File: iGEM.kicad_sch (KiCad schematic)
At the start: 49 parts, among them IC1 TMCS1107A1BQDRQ1, IC2 MCP4561-502E_MS, IC3 SN74LVC2G08IDCTRQ1, J1 COIL1, J2 Conn_01x03, J3 Conn_01x02, J4 Conn_01x03, J5 Conn_01x03, J6 Conn_02x03_Odd_Even, M1 Fan, Q1 TIP122, Q2 IPD042P03L3GATMA1, Q3 IPD042P03L3GATMA1, Q4 D44VH, Q5 IPD042P03L3GATMA1, Q6 IPD042P03L3GATMA1, U1 ADC101C021CIMK, U2 ATtiny412-SS, U3 SN74LVC1G04DBVR, U4 MD1211, U5 MD1211

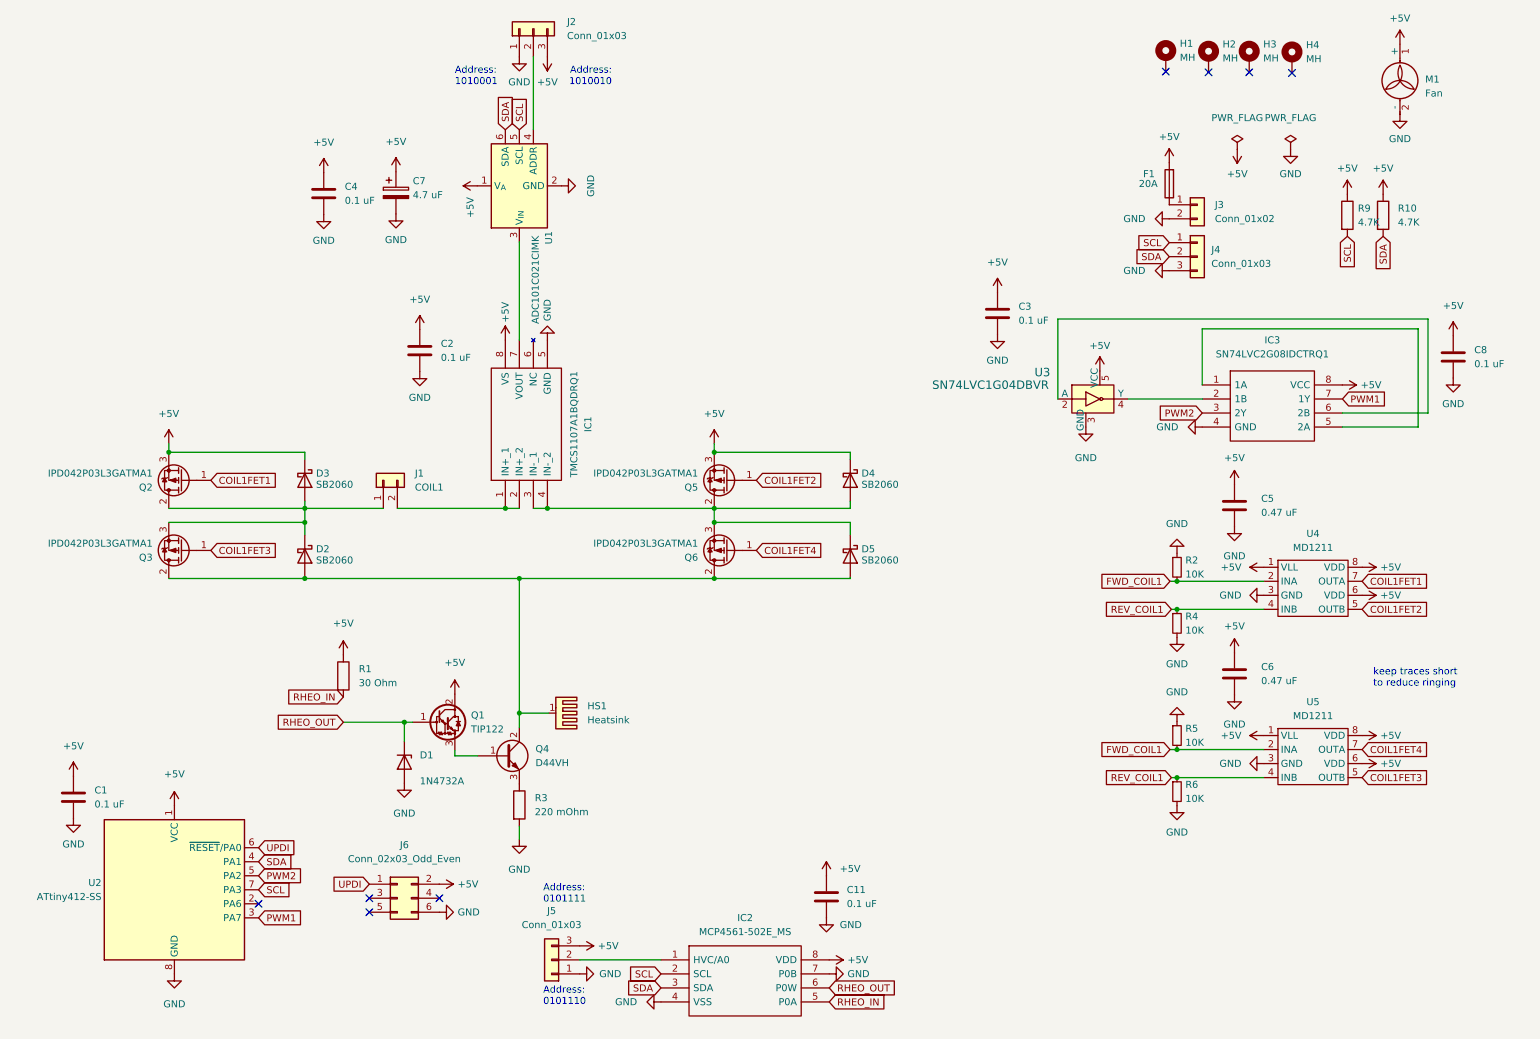
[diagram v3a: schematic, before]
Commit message: Added indicator LED and updated resistor value
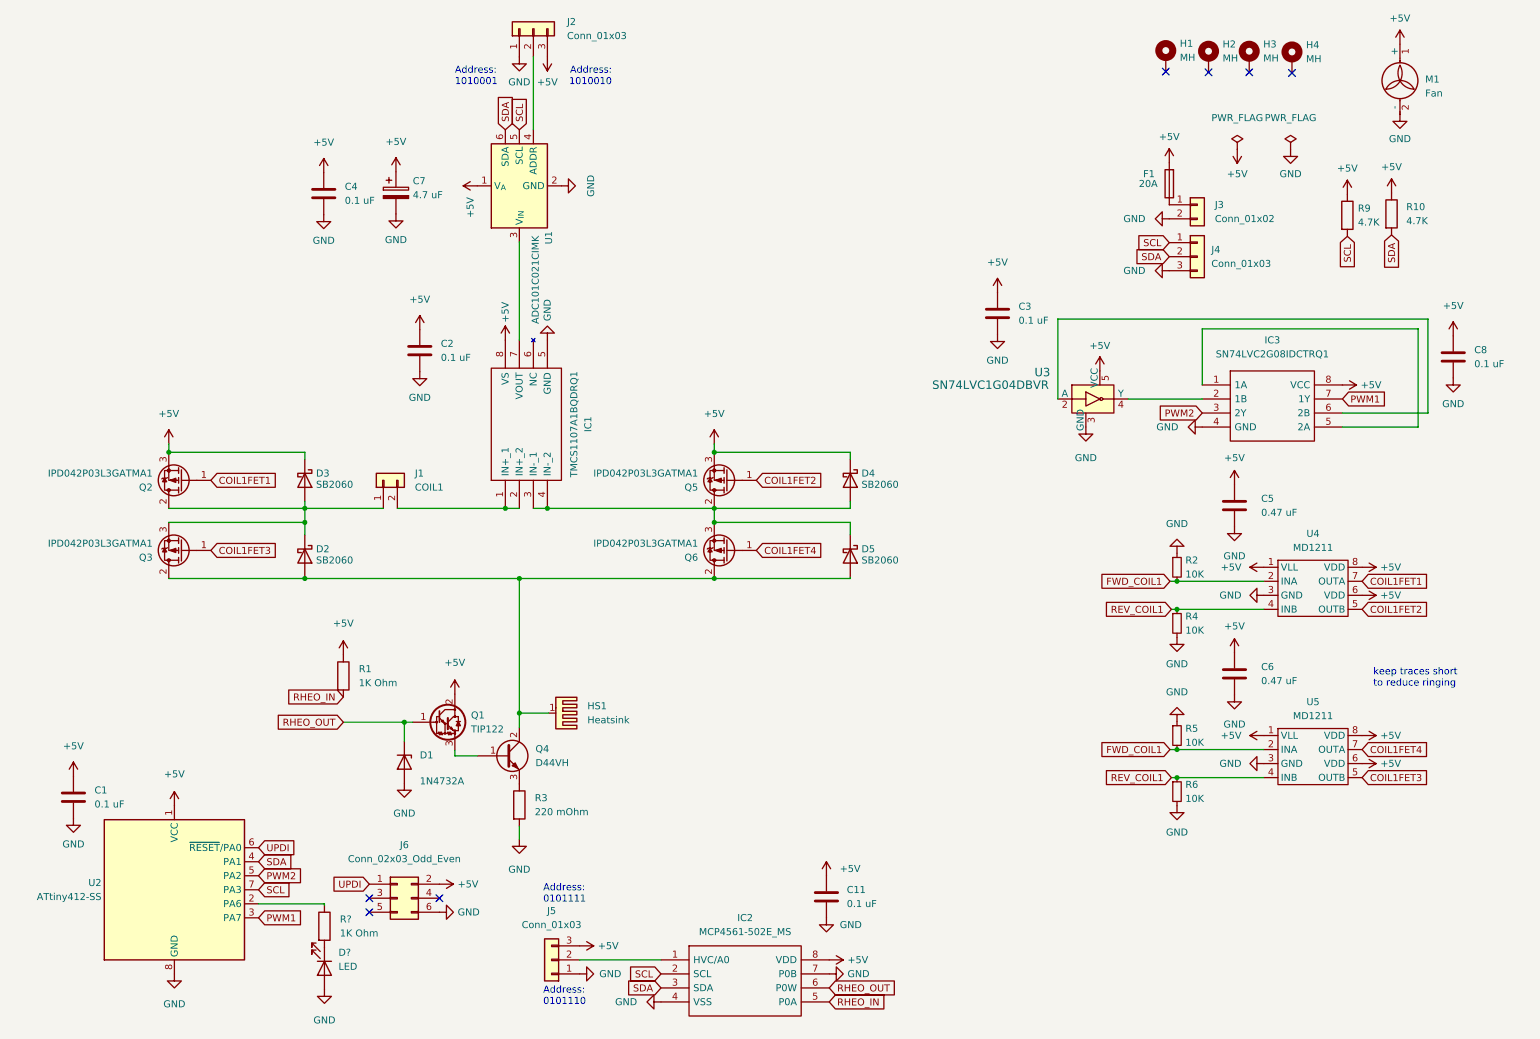
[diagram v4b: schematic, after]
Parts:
- added D?: LED, LED_SMD:LED_0805_2012Metric_Pad1.15x1.40mm_HandSolder, symbol Device:LED
- added R?: 1K Ohm, Resistor_SMD:R_0805_2012Metric_Pad1.20x1.40mm_HandSolder, symbol Device:R
- R1: value 30 Ohm -> 1K Ohm; footprint Capacitor_SMD:C_0805_2012Metric_Pad1.18x1.45mm_HandSolder -> Resistor_SMD:R_0805_2012Metric_Pad1.20x1.40mm_HandSolder; DigiKey RMCF0805FT30R0CT-ND -> CHP0805-FX-1001ELFCT-ND
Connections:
- net GND: now also D?.2 (A)
- net at U2.2 (PA6): now also R?.1
- new net: D?.1 (K), R?.2
- no-connect marks 8 -> 7
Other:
- moved on the sheet: R10
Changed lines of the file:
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@@
   (no_connect (at 236.093 24.638))
   (no_connect (at 243.84 24.765))
-  (no_connect (at 56.642 175.26))
   (wire (pts (xy 114.808 185.42) (xy 129.54 185.42))
     (stroke (width 0) (type default) (color 0 0 0 0))
@@
     (stroke (width 0) (type default) (color 0 0 0 0))
   )
+  (wire (pts (xy 68.58 175.26) (xy 68.58 175.514))
+    (stroke (width 0) (type default) (color 0 0 0 0))
+  )
   (wire (pts (xy 65.024 103.632) (xy 65.024 106.172))
     (stroke (width 0) (type default) (color 0 0 0 0))
@@
   )
   (wire (pts (xy 221.996 121.92) (xy 223.012 121.92))
+    (stroke (width 0) (type default) (color 0 0 0 0))
+  )
+  (wire (pts (xy 56.642 175.26) (xy 68.58 175.26))
     (stroke (width 0) (type default) (color 0 0 0 0))
   )
@@
     )
   )
-  (global_label "SDA" (shape input) (at 260.35 54.356 270) (fields_autoplaced)
+  (global_label "SDA" (shape input) (at 261.874 54.102 270) (fields_autoplaced)
     (effects (font (size 1.27 1.27)) (justify right))
-    (property "Intersheet References" "${INTERSHEET_REFS}" (id 0) (at 260.2706 60.3372 90)
+    (property "Intersheet References" "${INTERSHEET_REFS}" (id 0) (at 261.7946 60.0832 90)
       (effects (font (size 1.27 1.27)) (justify right) hide)
     )
@@
     (pin "3")
   )
-  (symbol (lib_id "Device:R") (at 260.35 50.546 0) (unit 1)
-    (in_bom yes) (on_board yes) (fields_autoplaced)
-    (property "Reference" "R10" (id 0) (at 263.017 49.2759 0)
-      (effects (font (size 1.27 1.27)) (justify left))
-    )
-    (property "Value" "4.7K" (id 1) (at 263.017 51.8159 0)
-      (effects (font (size 1.27 1.27)) (justify left))
-    )
-    (property "Footprint" "Resistor_SMD:R_0805_2012Metric_Pad1.20x1.40mm_HandSolder" (id 2) (at 258.572 50.546 90)
-      (effects (font (size 1.27 1.27)) hide)
-    )
-    (property "Datasheet" "~" (id 3) (at 260.35 50.546 0)
-      (effects (font (size 1.27 1.27)) hide)
-    )
-    (property "DigiKey" "RMCF0805FT4K70CT-ND" (id 4) (at 260.35 50.546 0)
+  (symbol (lib_id "Device:R") (at 261.874 50.292 0) (unit 1)
+    (in_bom yes) (on_board yes) (fields_autoplaced)
+    (property "Reference" "R10" (id 0) (at 264.541 49.0219 0)
+      (effects (font (size 1.27 1.27)) (justify left))
+    )
+    (property "Value" "4.7K" (id 1) (at 264.541 51.5619 0)
+      (effects (font (size 1.27 1.27)) (justify left))
+    )
+    (property "Footprint" "Resistor_SMD:R_0805_2012Metric_Pad1.20x1.40mm_HandSolder" (id 2) (at 260.096 50.292 90)
+      (effects (font (size 1.27 1.27)) hide)
+    )
+    (property "Datasheet" "~" (id 3) (at 261.874 50.292 0)
+      (effects (font (size 1.27 1.27)) hide)
+    )
+    (property "DigiKey" "RMCF0805FT4K70CT-ND" (id 4) (at 261.874 50.292 0)
       (effects (font (size 1.27 1.27)) hide)
     )
@@
     )
     (pin "1")
+  )
+  (symbol (lib_id "Device:LED") (at 68.58 186.944 270) (unit 1)
+    (in_bom yes) (on_board yes) (fields_autoplaced)
+    (property "Reference" "D?" (id 0) (at 71.12 184.0864 90)
+      (effects (font (size 1.27 1.27)) (justify left))
+    )
+    (property "Value" "LED" (id 1) (at 71.12 186.6264 90)
+      (effects (font (size 1.27 1.27)) (justify left))
+    )
+    (property "Footprint" "LED_SMD:LED_0805_2012Metric_Pad1.15x1.40mm_HandSolder" (id 2) (at 68.58 186.944 0)
+      (effects (font (size 1.27 1.27)) hide)
+    )
+    (property "Datasheet" "~" (id 3) (at 68.58 186.944 0)
+      (effects (font (size 1.27 1.27)) hide)
+    )
+    (property "DigiKey" "475-1410-1-ND" (id 4) (at 68.58 186.944 90)
+      (effects (font (size 1.27 1.27)) hide)
+    )
+    (pin "1")
+    (pin "2")
   )
   (symbol (lib_name "MD1211_1") (lib_id "MD1211:MD1211") (at 247.65 118.11 0) (unit 1)
@@
     (pin "2")
   )
-  (symbol (lib_id "power:+5V") (at 260.35 46.736 0) (unit 1)
+  (symbol (lib_id "power:+5V") (at 261.874 46.482 0) (unit 1)
     (in_bom yes) (on_board yes)
-    (property "Reference" "#PWR0119" (id 0) (at 260.35 50.546 0)
-      (effects (font (size 1.27 1.27)) hide)
-    )
-    (property "Value" "+5V" (id 1) (at 260.35 42.037 0))
-    (property "Footprint" "" (id 2) (at 260.35 46.736 0)
-      (effects (font (size 1.27 1.27)) hide)
-    )
-    (property "Datasheet" "" (id 3) (at 260.35 46.736 0)
+    (property "Reference" "#PWR0119" (id 0) (at 261.874 50.292 0)
+      (effects (font (size 1.27 1.27)) hide)
+    )
+    (property "Value" "+5V" (id 1) (at 261.874 41.783 0))
+    (property "Footprint" "" (id 2) (at 261.874 46.482 0)
+      (effects (font (size 1.27 1.27)) hide)
+    )
+    (property "Datasheet" "" (id 3) (at 261.874 46.482 0)
       (effects (font (size 1.27 1.27)) hide)
     )
@@
       (effects (font (size 1.27 1.27)) (justify left))
     )
-    (property "Value" "30 Ohm" (id 1) (at 74.803 135.2549 0)
-      (effects (font (size 1.27 1.27)) (justify left))
-    )
-    (property "Footprint" "Capacitor_SMD:C_0805_2012Metric_Pad1.18x1.45mm_HandSolder" (id 2) (at 70.231 133.985 90)
+    (property "Value" "1K Ohm" (id 1) (at 74.803 135.2549 0)
+      (effects (font (size 1.27 1.27)) (justify left))
+    )
+    (property "Footprint" "Resistor_SMD:R_0805_2012Metric_Pad1.20x1.40mm_HandSolder" (id 2) (at 70.231 133.985 90)
       (effects (font (size 1.27 1.27)) hide)
     )
@@
       (effects (font (size 1.27 1.27)) hide)
     )
-    (property "DigiKey" "RMCF0805FT30R0CT-ND" (id 4) (at 72.009 133.985 0)
+    (property "DigiKey" "CHP0805-FX-1001ELFCT-ND" (id 4) (at 72.009 133.985 0)
       (effects (font (size 1.27 1.27)) hide)
     )
@@
     (pin "1")
   )
+  (symbol (lib_id "power:GND") (at 68.58 190.754 0) (unit 1)
+    (in_bom yes) (on_board yes) (fields_autoplaced)
+    (property "Reference" "#PWR?" (id 0) (at 68.58 197.104 0)
+      (effects (font (size 1.27 1.27)) hide)
+    )
+    (property "Value" "GND" (id 1) (at 68.58 196.342 0))
+    (property "Footprint" "" (id 2) (at 68.58 190.754 0)
+      (effects (font (size 1.27 1.27)) hide)
+    )
+    (property "Datasheet" "" (id 3) (at 68.58 190.754 0)
+      (effects (font (size 1.27 1.27)) hide)
+    )
+    (pin "1")
+  )
   (symbol (lib_id "power:+5V") (at 256.54 119.38 270) (unit 1)
     (in_bom yes) (on_board yes) (fields_autoplaced)
@@
     (pin "1")
   )
+  (symbol (lib_id "Device:R") (at 68.58 179.324 0) (unit 1)
+    (in_bom yes) (on_board yes) (fields_autoplaced)
+    (property "Reference" "R?" (id 0) (at 71.374 178.0539 0)
+      (effects (font (size 1.27 1.27)) (justify left))
+    )
+    (property "Value" "1K Ohm" (id 1) (at 71.374 180.5939 0)
+      (effects (font (size 1.27 1.27)) (justify left))
+    )
+    (property "Footprint" "Resistor_SMD:R_0805_2012Metric_Pad1.20x1.40mm_HandSolder" (id 2) (at 66.802 179.324 90)
+      (effects (font (size 1.27 1.27)) hide)
+    )
+    (property "Datasheet" "~" (id 3) (at 68.58 179.324 0)
+      (effects (font (size 1.27 1.27)) hide)
+    )
+    (property "DigiKey" "CHP0805-FX-1001ELFCT-ND" (id 4) (at 68.58 179.324 0)
+      (effects (font (size 1.27 1.27)) hide)
+    )
+    (pin "1")
+    (pin "2")
+  )
   (symbol (lib_id "power:GND") (at 89.408 176.784 90) (unit 1)
     (in_bom yes) (on_board yes) (fields_autoplaced)
@@
       (reference "#PWR0131") (unit 1) (value "GND") (footprint "")
     )
+    (path "/c7e90eee-2fb5-4f34-8810-8edfe8f37c3a"
+      (reference "#PWR?") (unit 1) (value "GND") (footprint "")
+    )
     (path "/0fbdd8b7-d3db-4cb1-9102-673f223a760c"
       (reference "C1") (unit 1) (value "0.1 uF") (footprint "Capacitor_SMD:C_0805_2012Metric_Pad1.18x1.45mm_HandSolder")
@@
       (reference "D5") (unit 1) (value "SB2060") (footprint "Diode_THT:D_DO-201AD_P12.70mm_Horizontal")
     )
+    (path "/5327e8bf-ae82-4039-9cd4-8576c3288851"
+      (reference "D?") (unit 1) (value "LED") (footprint "LED_SMD:LED_0805_2012Metric_Pad1.15x1.40mm_HandSolder")
+    )
     (path "/eadcb800-30ab-4a2d-bc96-28b421a136a3"
       (reference "F1") (unit 1) (value "20A") (footprint "Fuse:Fuseholder_Blade_Mini_Keystone_3568")
@@
     )
     (path "/9dbd19f4-6a66-4910-871d-92295a4321e7"
-      (reference "R1") (unit 1) (value "30 Ohm") (footprint "Capacitor_SMD:C_0805_2012Metric_Pad1.18x1.45mm_HandSolder")
+      (reference "R1") (unit 1) (value "1K Ohm") (footprint "Resistor_SMD:R_0805_2012Metric_Pad1.20x1.40mm_HandSolder")
     )
     (path "/82e4ca13-c8a3-4875-a498-8c74cd9a9fd2"
@@
       (reference "R10") (unit 1) (value "4.7K") (footprint "Resistor_SMD:R_0805_2012Metric_Pad1.20x1.40mm_HandSolder")
     )
+    (path "/e621144d-f4f0-4ed0-afcb-e43069706fe3"
+      (reference "R?") (unit 1) (value "1K Ohm") (footprint "Resistor_SMD:R_0805_2012Metric_Pad1.20x1.40mm_HandSolder")
+    )
     (path "/69a61c1d-1543-4184-a789-f583b0735f7e"

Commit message: added bulk capacitance and bug fixes
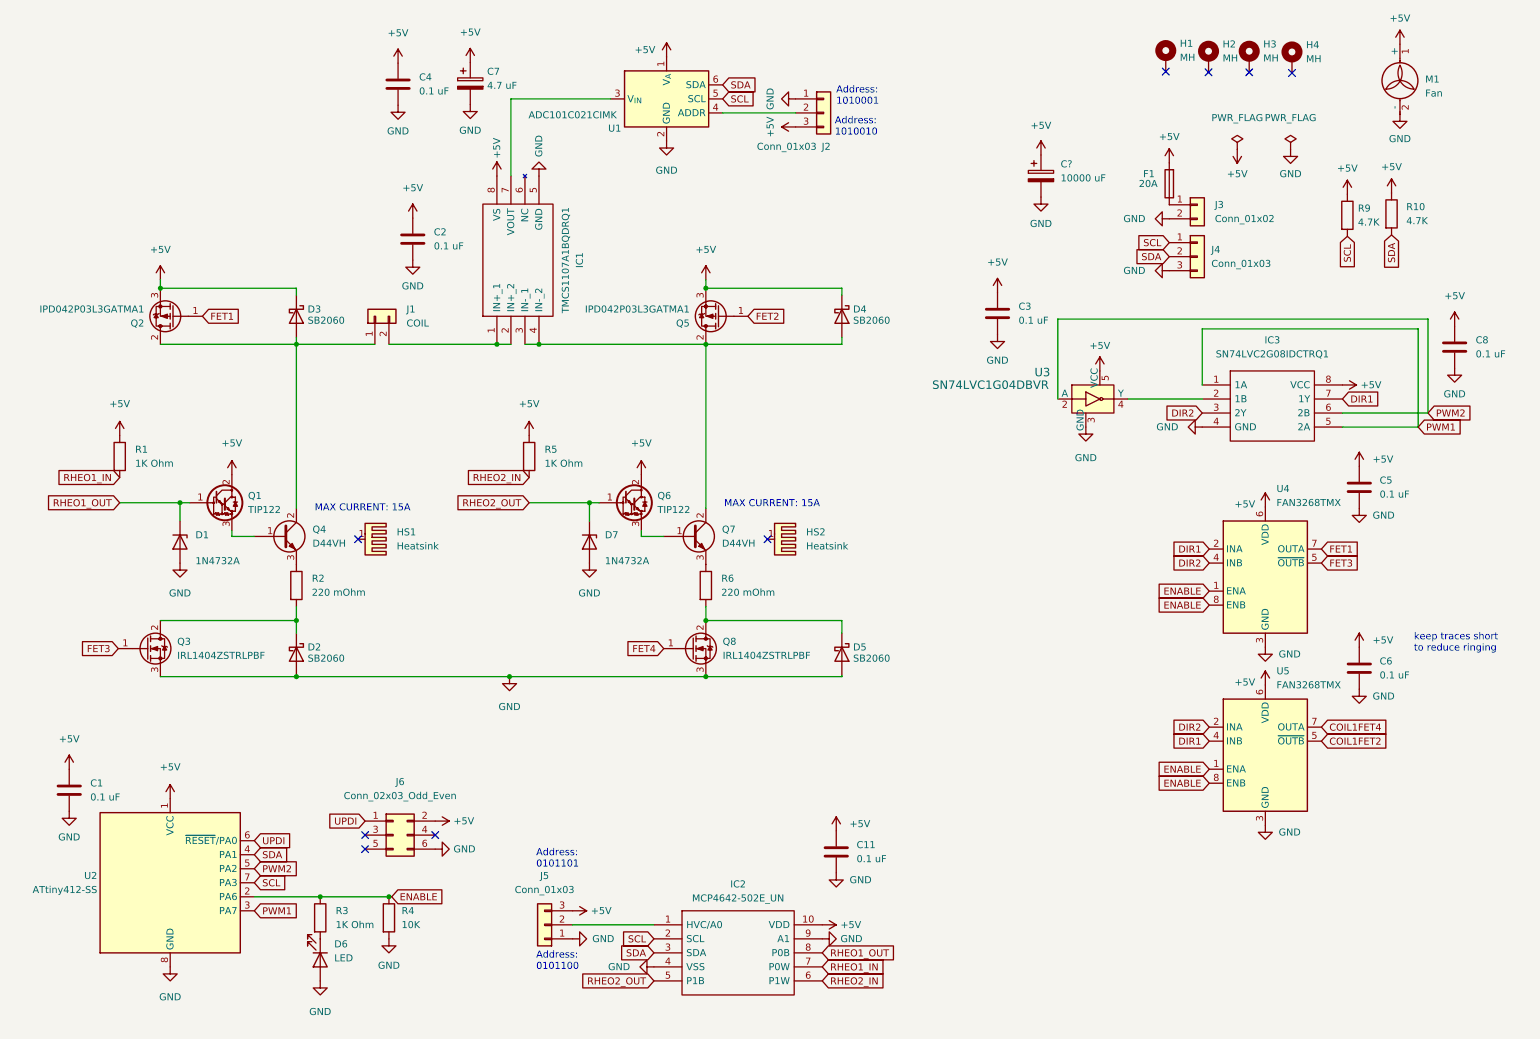
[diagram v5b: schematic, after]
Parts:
- removed IC2: MCP4561-502E_MS, Package_SO:MSOP-8_3x3mm_P0.65mm, symbol MCP4561-502E_MS:MCP4561-502E_MS
- removed Q3, Q6: IPD042P03L3GATMA1, Package_TO_SOT_SMD:TO-252-2, symbol Device:Q_PMOS_GDS
- removed R2, R4, R5, R6: 10K, Capacitor_SMD:C_0805_2012Metric_Pad1.18x1.45mm_HandSolder, symbol Device:R_Small
- removed R3: 220 mOhm, TerminalBlock:TerminalBlock_bornier-2_P5.08mm, symbol Device:R
- removed U4, U5: MD1211, Package_SO:SOIC-8_3.9x4.9mm_P1.27mm, symbol MD1211:MD1211
- added C?: 10000 uF, Capacitor_THT:CP_Radial_D22.0mm_P10.00mm_SnapIn, symbol Device:C_Polarized
- added D7: 1N4732A, Diode_THT:D_DO-41_SOD81_P10.16mm_Horizontal, symbol Diode:1N47xxA
- added HS2: Heatsink, Heatsink:Heatsink_AAVID_576802B03900G, symbol Mechanical:Heatsink_Pad
- added IC2: MCP4642-502E_UN, SOP50P490X110-10N, symbol MCP4642-502E_UN:MCP4642-502E_UN
- added Q3, Q8: IRL1404ZSTRLPBF, Package_TO_SOT_SMD:TO-263-2, symbol Device:Q_NMOS_GDS
- added Q6: TIP122, Package_TO_SOT_THT:TO-220-3_Vertical, symbol Transistor_BJT:TIP122
- added Q7: D44VH, Package_TO_SOT_THT:TO-220-3_Vertical, symbol Device:Q_NPN_BCE
- added R2, R6: 220 mOhm, TerminalBlock:TerminalBlock_bornier-2_P5.08mm, symbol Device:R
- added R4: 10K, Resistor_SMD:R_0805_2012Metric_Pad1.20x1.40mm_HandSolder, symbol Device:R
- added R5: 1K Ohm, Resistor_SMD:R_0805_2012Metric_Pad1.20x1.40mm_HandSolder, symbol Device:R
- added U4, U5: FAN3268TMX, Package_SO:SOIC-8_3.9x4.9mm_P1.27mm, symbol Driver_FET:FAN3268
- C5, C6: value 0.47 uF -> 0.1 uF; DigiKey 399-C0805C474K8RAC7800CT-ND -> 399-C0805C104K8RAC7800CT-ND
- J1: value COIL1 -> COIL
- gave numbers to parts that had none: 2
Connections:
- net +5V: now also C?.1, IC2.10 (VDD), Q6.2 (C), R5.1, U4.6 (VDD), U5.6 (VDD)
- net COIL1FET2: now also U5.5 (~{OUTB}); no longer Q5.1 (G)
- net COIL1FET4: now also U5.7 (OUTA)
- net GND: now also D2.2 (A), D5.2 (A), C?.2, D7.2 (A), IC2.4 (VSS), IC2.9 (A1), Q3.3 (S), Q8.3 (S), R4.2, U4.3 (GND), U5.3 (GND)
- net PWM1: now also IC3.1 (1A), IC3.5 (2A); no longer IC3.7 (1Y)
- net PWM2: now also IC3.6 (2B), U3.2 (A); no longer IC3.3 (2Y)
- net SCL: now also IC2.2 (SCL)
- net SDA: now also IC2.3 (SDA)
- net at J5.2 (Pin_2): now also IC2.1 (HVC/A0)
- net at D4.2 (A), IC1.3 (IN-_1), IC1.4 (IN-_2)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: now also Q7.2 (C); no longer D5.1 (K)
- net at D3.2 (A), J1.1 (Pin_1), Q2.2 (D): now also Q4.2 (C); no longer D2.1 (K)
- net at Q4.3 (E): now also R2.1
- net ENABLE: now reaches R3.1, U2.2 (PA6)
- net ENABLE: now also R4.1, U4.1 (ENA), U4.8 (ENB), U5.1 (ENA), U5.8 (ENB)
- net COIL1FET1 renamed FET1
- net FET1: now also U4.7 (OUTA)
- net RHEO_IN renamed RHEO1_IN
- net RHEO1_IN: now also IC2.7 (P0W)
- net RHEO_OUT renamed RHEO1_OUT
- net RHEO1_OUT: now also IC2.8 (P0B)
- new net: D2.1 (K), Q3.2 (D), R2.2
- new net: Q6.3 (E), Q7.1 (B)
- new net: Q7.3 (E), R6.1
- new net: D5.1 (K), Q8.2 (D), R6.2
- new net DIR1: IC3.7 (1Y), U4.2 (INA), U5.4 (INB)
- new net DIR2: IC3.3 (2Y), U4.4 (INB), U5.2 (INA)
- new net FET2: Q5.1 (G)
- new net FET3: Q3.1 (G), U4.5 (~{OUTB})
- new net FET4: Q8.1 (G)
- new net RHEO2_IN: IC2.6 (P1W), R5.2
- new net RHEO2_OUT: D7.1 (K), IC2.5 (P1B), Q6.1 (B)
- now unconnected: HS1.1
- no-connect marks 7 -> 9
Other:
- note added: "Address: 0101100"
- note added: "Address: 0101101"
- note added: "MAX CURRENT: 15A"
- note removed: "Address: 0101110"
- note removed: "Address: 0101111"
- moved on the sheet: C1, C11, C2, C4, C7, C8, D1, D2, D3, D4, D5, D6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
